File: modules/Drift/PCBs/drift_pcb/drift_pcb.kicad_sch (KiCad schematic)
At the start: 8 parts, among them J4 Conn_01x06_Pin, J5 Conn_01x06_Socket, J6 Conn_01x04_Pin, J7 Conn_01x04_Socket, J9 Eurorack_2x8_Power

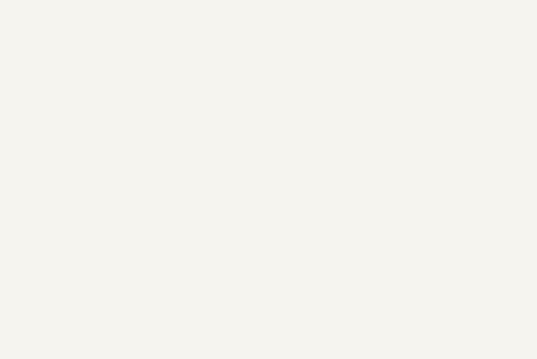
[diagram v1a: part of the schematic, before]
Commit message: Add mounting hole, clean up layout
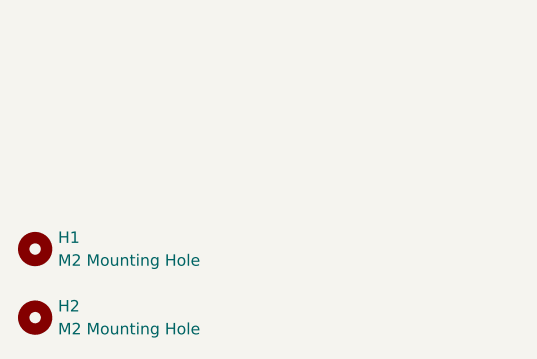
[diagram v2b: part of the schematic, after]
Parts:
- added H1, H2: M2 Mounting Hole, MountingHole:MountingHole_2.2mm_M2, symbol Mechanical:MountingHole
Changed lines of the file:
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@@
 		(title "Drift")
 		(date "2024-08-13")
-		(rev "v0.2")
+		(rev "v1.0")
 		(company "Free Modular")
 	)
@@
 			(width 0)
 			(type default)
+		)
+	)
+	(symbol
+		(lib_id "Mechanical:MountingHole")
+		(at 35.56 162.56 0)
+		(unit 1)
+		(exclude_from_sim yes)
+		(in_bom no)
+		(on_board yes)
+		(dnp no)
+		(fields_autoplaced yes)
+		(property "Reference" "H1"
+			(at 38.1 161.2899 0)
+			(effects
+				(font
+					(size 1.27 1.27)
+				)
+				(justify left)
+			)
+		)
+		(property "Value" "M2 Mounting Hole"
+			(at 38.1 163.8299 0)
+			(effects
+				(font
+					(size 1.27 1.27)
+				)
+				(justify left)
+			)
+		)
+		(property "Footprint" "MountingHole:MountingHole_2.2mm_M2"
+			(at 35.56 162.56 0)
+			(effects
+				(font
+					(size 1.27 1.27)
+				)
+				(hide yes)
+			)
+		)
+		(property "Datasheet" "~"
+			(at 35.56 162.56 0)
+			(effects
+				(font
+					(size 1.27 1.27)
+				)
+				(hide yes)
+			)
+		)
+		(property "Description" "Mounting Hole without connection"
+			(at 35.56 162.56 0)
+			(effects
+				(font
+					(size 1.27 1.27)
+				)
+				(hide yes)
+			)
+		)
+		(instances
+			(project ""
+				(path "/aac2b9ae-0367-4446-b109-7473284ab08d"
+					(reference "H1")
+					(unit 1)
+				)
+			)
 		)
 	)
@@
 					(unit 1)
 				)
+			)
+		)
+	)
+	(symbol
+		(lib_id "Mechanical:MountingHole")
+		(at 35.56 170.18 0)
+		(unit 1)
+		(exclude_from_sim yes)
+		(in_bom no)
+		(on_board yes)
+		(dnp no)
+		(fields_autoplaced yes)
+		(property "Reference" "H2"
+			(at 38.1 168.9099 0)
+			(effects
+				(font
+					(size 1.27 1.27)
+				)
+				(justify left)
+			)
+		)
+		(property "Value" "M2 Mounting Hole"
+			(at 38.1 171.4499 0)
+			(effects
+				(font
+					(size 1.27 1.27)
+				)
+				(justify left)
+			)
+		)
+		(property "Footprint" "MountingHole:MountingHole_2.2mm_M2"
+			(at 35.56 170.18 0)
+			(effects
+				(font
+					(size 1.27 1.27)
+				)
+				(hide yes)
+			)
+		)
+		(property "Datasheet" "~"
+			(at 35.56 170.18 0)
+			(effects
+				(font
+					(size 1.27 1.27)
+				)
+				(hide yes)
+			)
+		)
+		(property "Description" "Mounting Hole without connection"
+			(at 35.56 170.18 0)
+			(effects
+				(font
+					(size 1.27 1.27)
+				)
+				(hide yes)
+			)
+		)
+		(instances
+			(project "drift_pcb"
+				(path "/aac2b9ae-0367-4446-b109-7473284ab08d"
+					(reference "H2")
+					(unit 1)
+				)

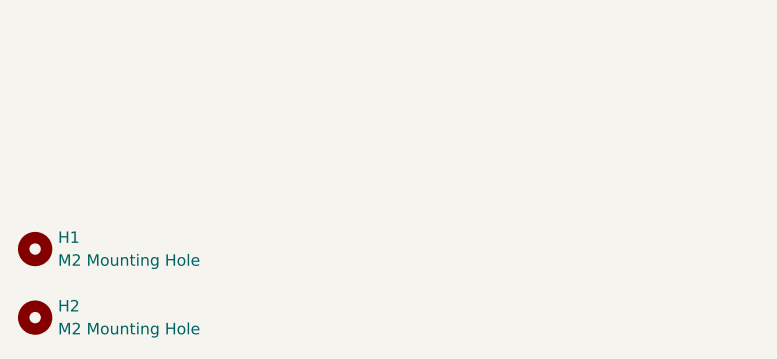
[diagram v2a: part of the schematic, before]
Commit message: Add second mounting hole to Drift
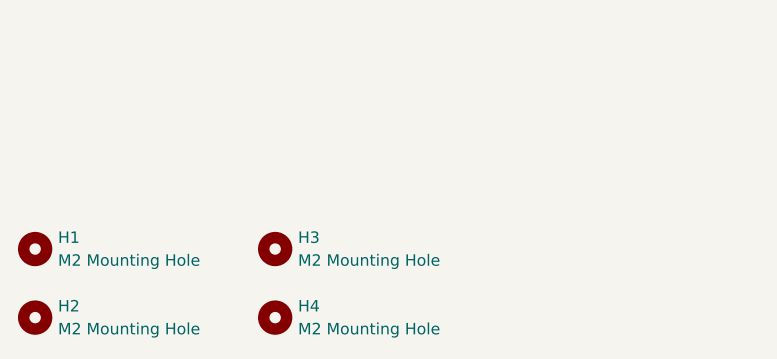
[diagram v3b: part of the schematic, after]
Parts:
- added H3, H4: M2 Mounting Hole, MountingHole:MountingHole_2.2mm_M2, symbol Mechanical:MountingHole
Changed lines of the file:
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@@
+	)
+	(symbol
+		(lib_id "Mechanical:MountingHole")
+		(at 62.23 162.56 0)
+		(unit 1)
+		(exclude_from_sim yes)
+		(in_bom no)
+		(on_board yes)
+		(dnp no)
+		(fields_autoplaced yes)
+		(property "Reference" "H3"
+			(at 64.77 161.2899 0)
+			(effects
+				(font
+					(size 1.27 1.27)
+				)
+				(justify left)
+			)
+		)
+		(property "Value" "M2 Mounting Hole"
+			(at 64.77 163.8299 0)
+			(effects
+				(font
+					(size 1.27 1.27)
+				)
+				(justify left)
+			)
+		)
+		(property "Footprint" "MountingHole:MountingHole_2.2mm_M2"
+			(at 62.23 162.56 0)
+			(effects
+				(font
+					(size 1.27 1.27)
+				)
+				(hide yes)
+			)
+		)
+		(property "Datasheet" "~"
+			(at 62.23 162.56 0)
+			(effects
+				(font
+					(size 1.27 1.27)
+				)
+				(hide yes)
+			)
+		)
+		(property "Description" "Mounting Hole without connection"
+			(at 62.23 162.56 0)
+			(effects
+				(font
+					(size 1.27 1.27)
+				)
+				(hide yes)
+			)
+		)
+		(instances
+			(project "drift_pcb"
+				(path "/aac2b9ae-0367-4446-b109-7473284ab08d"
+					(reference "H3")
+					(unit 1)
+				)
+			)
+		)
 	)
 	(symbol
@@
 					(unit 1)
 				)
+			)
+		)
+	)
+	(symbol
+		(lib_id "Mechanical:MountingHole")
+		(at 62.23 170.18 0)
+		(unit 1)
+		(exclude_from_sim yes)
+		(in_bom no)
+		(on_board yes)
+		(dnp no)
+		(fields_autoplaced yes)
+		(property "Reference" "H4"
+			(at 64.77 168.9099 0)
+			(effects
+				(font
+					(size 1.27 1.27)
+				)
+				(justify left)
+			)
+		)
+		(property "Value" "M2 Mounting Hole"
+			(at 64.77 171.4499 0)
+			(effects
+				(font
+					(size 1.27 1.27)
+				)
+				(justify left)
+			)
+		)
+		(property "Footprint" "MountingHole:MountingHole_2.2mm_M2"
+			(at 62.23 170.18 0)
+			(effects
+				(font
+					(size 1.27 1.27)
+				)
+				(hide yes)
+			)
+		)
+		(property "Datasheet" "~"
+			(at 62.23 170.18 0)
+			(effects
+				(font
+					(size 1.27 1.27)
+				)
+				(hide yes)
+			)
+		)
+		(property "Description" "Mounting Hole without connection"
+			(at 62.23 170.18 0)
+			(effects
+				(font
+					(size 1.27 1.27)
+				)
+				(hide yes)
+			)
+		)
+		(instances
+			(project "drift_pcb"
+				(path "/aac2b9ae-0367-4446-b109-7473284ab08d"
+					(reference "H4")
+					(unit 1)
+				)
